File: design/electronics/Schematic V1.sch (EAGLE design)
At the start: 175 parts, among them J1 PJ-202AH, J2 PJ-025, J3 DD50P564GTXLF, J4 DD50P564GTXLF, J5 SAMTEC-TST-105-01-X-DJ, J6 SSW-106-02-TM-S-RA, SW1 TL6330AF200Q, U1 STM32F207VGT6TR, U10 SN65LBC175ADD16-M, U11 MAX7375AXR805+T21-0075D_MXM-M, U12 SN75ALS174ADWRDW20-M, U13 SN75468DRD0016A_M, U14 SN75468DRD0016A_M, U15 ACSL-6400-00TESOIC_6400-00TE-M, U16 ACSL-6400-00TESOIC_6400-00TE-M, U17 SN65LBC175ADD16-M, U18 SN65LBC175ADD16-M, U19 SN65LBC175ADD16-M, U2 LM2678S-5.0/NOPBTS7B-M, U21 RS0104YQTSSOP-14_JRT-M, U22 RS0104YQTSSOP-14_JRT-M, U24 RS0104YQTSSOP-14_JRT-M, U3 CDBC520-GCDBC-G-M, U4 TLV1117LV33DCYR, U5 STM32F207VGT6TR, U6 RS0104YQTSSOP-14_JRT-M, U7 SN75ALS174ADWRDW20-M, U8 OPA4205APWRTSSOP14_PW_R-PDSO-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, U9 TPS63700DRCR

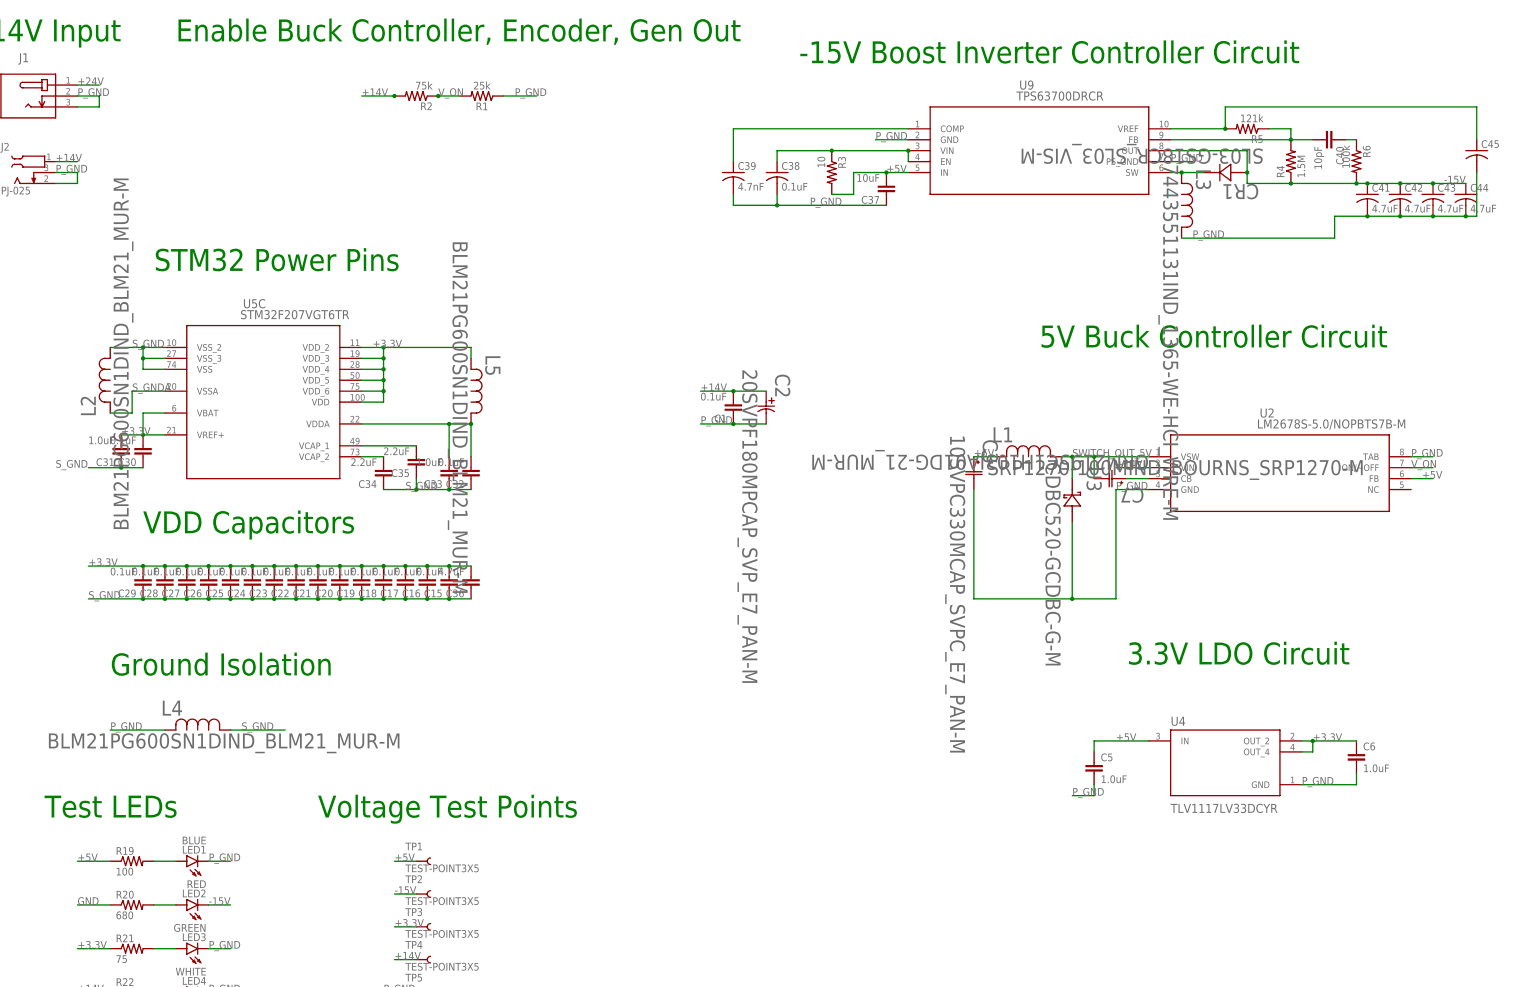
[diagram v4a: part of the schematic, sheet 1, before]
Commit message: Updated Power Circuit Schematic + Layout + Components
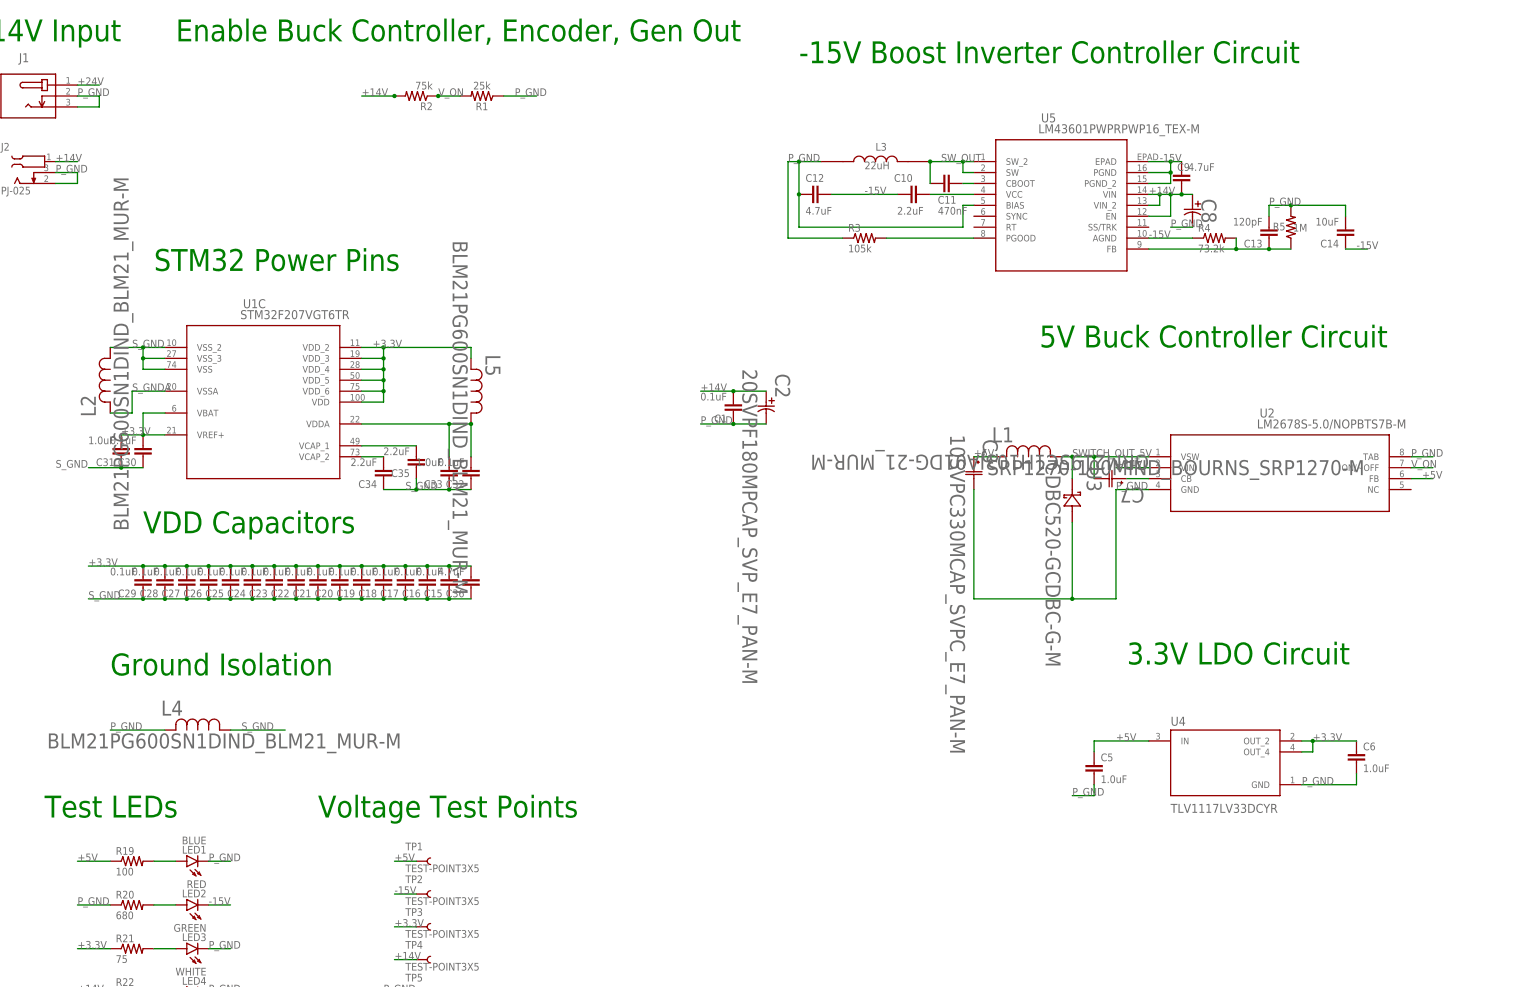
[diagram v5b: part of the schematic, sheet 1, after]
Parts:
- removed C37: 10uF, SparkFun-Capacitors:10UF-0805-10V-10%
- removed C38: 0.1uF, rcl:C-USC0805
- removed C39: 4.7nF, rcl:C-USC0805
- removed C40: 10pF, SparkFun-Capacitors:10UF-0805-10V-10%
- removed C41, C42, C43, C44: 4.7uF, rcl:C-USC0805
- removed C45: (no value), rcl:C-USC0805
- removed CR1: SL03-GS18CR_SL03_VIS-M, SSW-130-01-G-S:SL03-GS18CR_SL03_VIS-M
- removed R6: 100k, rcl:R-US_R0805
- removed U9: TPS63700DRCR, SSW-130-01-G-S:TPS63700DRCR
- added C10: 2.2uF, SparkFun-Capacitors:2.2UF-0805-25V-(+80/-20%)
- added C11: 470nF, SparkFun-Capacitors:470NF-0805-100V-10%-X7S
- added C12, C9: 4.7uF, SparkFun-Capacitors:4.7UF-0805-50V-(10%)
- added C13: 120pF, SparkFun-Capacitors:4.7UF-0805-50V-(10%)
- added C14: 10uF, SparkFun-Capacitors:4.7UF-0805-50V-(10%)
- added C8: 68uF, SSW-130-01-G-S:UWD1V680MCL1GSPCAP_6.3X7.7-ELECT_NCA-M
- L3: value 7443551131IND_1365-WE-HCI_WRE-M -> 22uH; device SSW-130-01-G-S:7443551131IND_1365-WE-HCI_WRE-M -> SSW-130-01-G-S:VLS201610CX-220M-1
- R3: value 10 -> 105k
- R4: value 1.5M -> 73.2k
- R5: value 121k -> 1M
- R69: value (none) -> 10k
- U5: value STM32F207VGT6TR -> LM43601PWPRPWP16_TEX-M; device SSW-130-01-G-S:STM32F207VGT6TR -> SSW-130-01-G-S:LM43601PWPRPWP16_TEX-M
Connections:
- removed net FRWD_EX_TORQUE_LIM_GPIO_1: U1A.PC6
- removed net FRWD_EX_TORQUE_LIM_GPIO_2: U1A.PA11
- removed net GND: R20.1
- removed net N$10: C40.2, R4.2, R5.1, U9.FB
- removed net N$6: C38.1, R3.1, U9.EN, U9.VIN
- removed net N$9: C45.1, R5.2, U9.VREF
- new net SW_OUT: C11.1, L3.2, U5.SW, U5.SW_2
- net +14V: now also C8.1, C9.2, U5.EN, U5.VIN, U5.VIN_2
- net +3.3V: now also U1C.VBAT, U1C.VDD, U1C.VDD_2, U1C.VDD_3, U1C.VDD_4, U1C.VDD_5, U1C.VDD_6, U1C.VREF+; no longer U5C.VBAT, U5C.VDD, U5C.VDD_2, U5C.VDD_3, U5C.VDD_4, U5C.VDD_5, U5C.VDD_6, U5C.VREF+
- net +5V: no longer C37.2, R3.2, U9.IN
- net -15V: now also C10.1, C12.1, C14.1, C9.1, U5.AGND, U5.EPAD, U5.PGND, U5.PGND_2; no longer C41.1, C42.1, C43.1, C44.1, CR1.2, R6.2, U9.OUT
- net EXT_CLK: now also U1B.PH0/OSC_IN
- net FRWD_EX_TORQUE_LIM_EN_GPIO_1: now also U1A.PC6
- net FRWD_EX_TORQUE_LIM_EN_GPIO_2: now also U1A.PA11
- net GEN_PURPOSE_OUT_GPIO_A_2: no longer U19.1Y
- net GEN_PURPOSE_OUT_GPIO_A_2_5V: now also U19.1Y
- net GEN_PURPOSE_OUT_GPIO_B_2: no longer U19.2Y
- net GEN_PURPOSE_OUT_GPIO_B_2_5V: now also U19.2Y
- net GEN_PURPOSE_OUT_GPIO_C_2: no longer U19.3Y
- net GEN_PURPOSE_OUT_GPIO_C_2_5V: now also U19.3Y
- net N$1: now also C10.2, U5.VCC; no longer U1B.PH0/OSC_IN
- net N$11: now also C13.1, R4.2, R5.1, U5.FB; no longer C40.1, R6.1
- net N$14: now also U1C.VDDA; no longer U5C.VDDA
- net N$3: now also C11.2, U5.CBOOT; no longer C39.1, U9.COMP
- net N$4: now also U1C.VCAP_1; no longer U5C.VCAP_1
- net N$5: now also U1C.VCAP_2; no longer U5C.VCAP_2
- net N$7: now also R3.2, U5.PGOOD; no longer CR1.1, L3.2, U9.SW
- net P_GND: now also C12.2, C13.2, C14.2, C8.2, R20.1, R3.1, R5.2, U5.BIAS; no longer C37.1, C38.2, C39.2, C41.2, C42.2, C43.2, C44.2, C45.2, U9.GND, U9.PS_GND
- net SERVO_ALARM_OUT_GPIO_2: no longer U19.4Y
- net SERVO_ALARM_OUT_GPIO_2_5V: now also U19.4Y
- net S_GND: now also U1C.VSS, U1C.VSS_2, U1C.VSS_3; no longer U5C.VSS, U5C.VSS_2, U5C.VSS_3
- net S_GNDA: now also U1C.VSSA; no longer U5C.VSSA
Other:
- moved on the sheet: R3, R4, R5

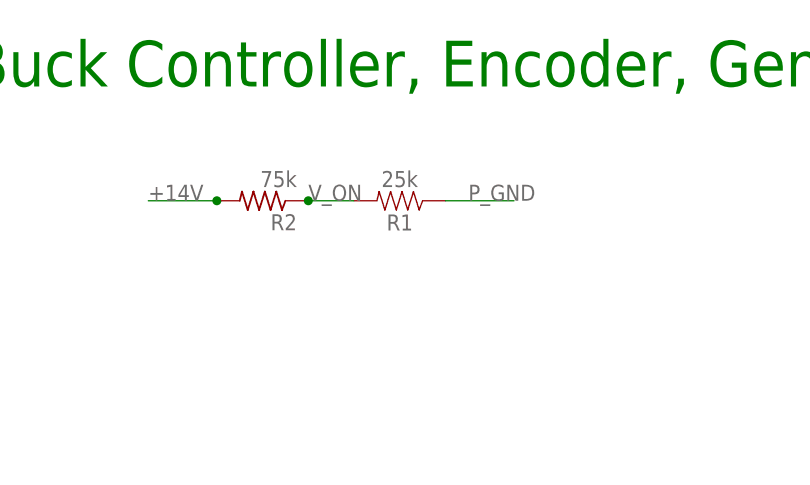
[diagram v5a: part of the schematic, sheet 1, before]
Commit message: Updated Schematic and Board with a few components
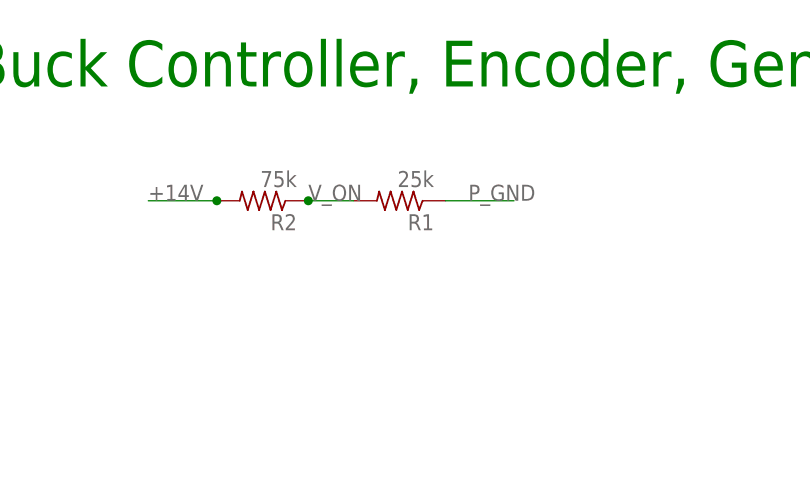
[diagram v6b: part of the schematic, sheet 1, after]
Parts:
- R1: device SparkFun-Resistors:33KOHM-0603-1/10W-1% -> rcl:R-US_R0805
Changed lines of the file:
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@@
 <part name="R15" library="rcl" library_urn="urn:adsk.eagle:library:334" deviceset="R-US_" device="R0805" package3d_urn="urn:adsk.eagle:package:23553/2" value="73k"/>
 <part name="R16" library="rcl" library_urn="urn:adsk.eagle:library:334" deviceset="R-US_" device="R0805" package3d_urn="urn:adsk.eagle:package:23553/2" value="10k"/>
-<part name="R1" library="SparkFun-Resistors" library_urn="urn:adsk.eagle:library:532" deviceset="33KOHM" device="-0603-1/10W-1%" package3d_urn="urn:adsk.eagle:package:39650/1" value="25k"/>
 <part name="R2" library="rcl" library_urn="urn:adsk.eagle:library:334" deviceset="R-US_" device="R0805" package3d_urn="urn:adsk.eagle:package:23553/2" value="75k"/>
 <part name="C46" library="SparkFun-Capacitors" library_urn="urn:adsk.eagle:library:510" deviceset="1.0UF" device="-0805-25V-10%" package3d_urn="urn:adsk.eagle:package:37429/1" value="1.0uF"/>
@@
 <part name="C13" library="SparkFun-Capacitors" deviceset="4.7UF" device="-0805-50V-(10%)" value="120pF"/>
 <part name="C14" library="SparkFun-Capacitors" deviceset="4.7UF" device="-0805-50V-(10%)" value="10uF"/>
+<part name="R1" library="rcl" library_urn="urn:adsk.eagle:library:334" deviceset="R-US_" device="R0805" package3d_urn="urn:adsk.eagle:package:23553/2" value="25k"/>
 </parts>
 <sheets>
@@
 <attribute name="NAME" x="32.1056" y="236.4486" size="2.0828" layer="95" ratio="6" rot="SR0"/>
 </instance>
-<instance part="R1" gate="G$1" x="139.7" y="228.6" smashed="yes" rot="R180">
-<attribute name="NAME" x="139.7" y="227.076" size="1.778" layer="95" font="vector" rot="R180" align="bottom-center"/>
-<attribute name="VALUE" x="139.7" y="230.124" size="1.778" layer="96" font="vector" rot="R180" align="top-center"/>
-</instance>
 <instance part="R2" gate="G$1" x="124.46" y="228.6" smashed="yes" rot="R180">
 <attribute name="NAME" x="128.27" y="227.1014" size="1.778" layer="95" rot="R180"/>
@@
 <attribute name="NAME" x="338.836" y="195.199" size="1.778" layer="95" font="vector" rot="R180"/>
 <attribute name="VALUE" x="338.836" y="200.279" size="1.778" layer="96" font="vector" rot="R180"/>
+</instance>
+<instance part="R1" gate="G$1" x="139.7" y="228.6" smashed="yes" rot="R180">
+<attribute name="NAME" x="143.51" y="227.1014" size="1.778" layer="95" rot="R180"/>
+<attribute name="VALUE" x="143.51" y="231.902" size="1.778" layer="96" rot="R180"/>
 </instance>
 </instances>
@@
 </segment>
 <segment>
-<pinref part="R1" gate="G$1" pin="1"/>
 <wire x1="144.78" y1="228.6" x2="152.4" y2="228.6" width="0.1524" layer="91"/>
 <label x="147.32" y="228.6" size="1.778" layer="95"/>
+<pinref part="R1" gate="G$1" pin="1"/>
 </segment>
 <segment>
@@
 </segment>
 <segment>
-<pinref part="R1" gate="G$1" pin="2"/>
 <wire x1="129.54" y1="228.6" x2="134.62" y2="228.6" width="0.1524" layer="91"/>
 <label x="129.54" y="228.6" size="1.778" layer="95"/>
 <pinref part="R2" gate="G$1" pin="1"/>
 <junction x="129.54" y="228.6"/>
+<pinref part="R1" gate="G$1" pin="2"/>
 </segment>
 </net>

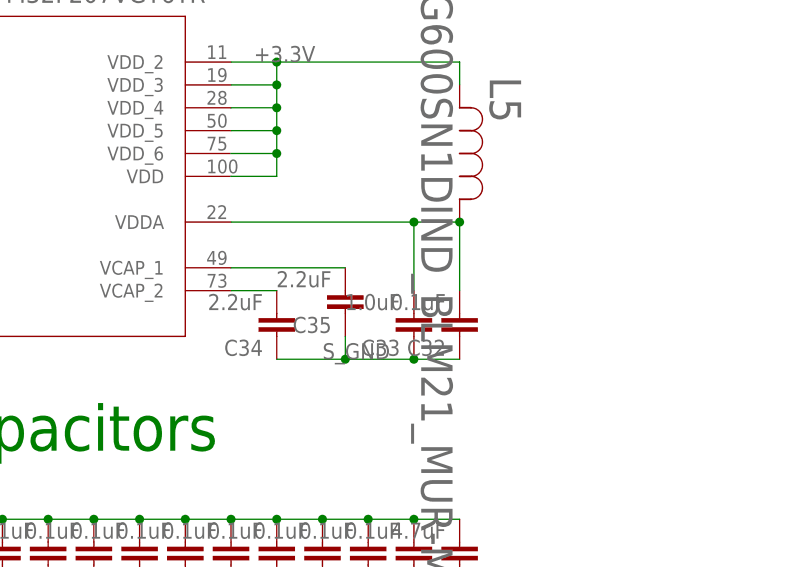
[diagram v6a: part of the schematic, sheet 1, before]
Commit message: Updated Power Scheme of STM32
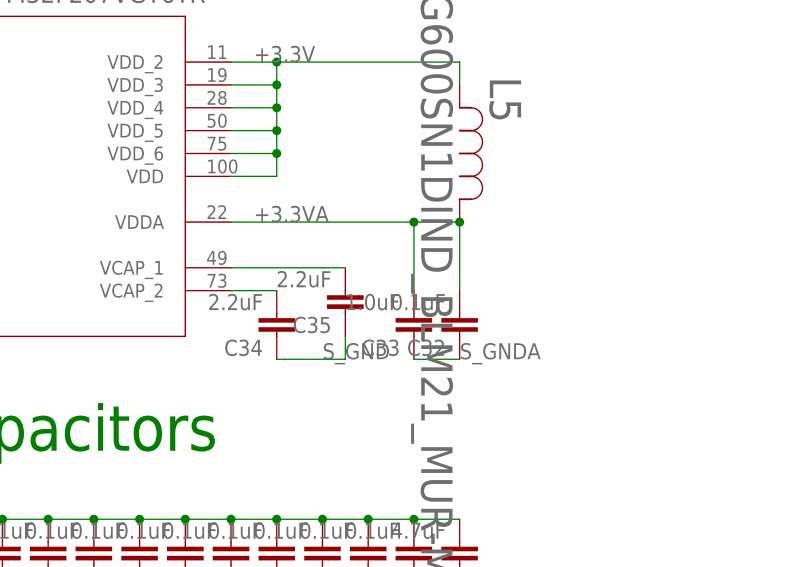
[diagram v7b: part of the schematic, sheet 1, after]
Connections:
- net N$14 renamed +3.3VA
- net S_GND: no longer C32.1, C33.1
- net S_GNDA: now also C32.1, C33.1
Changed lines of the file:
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@@
 <wire x1="124.46" y1="137.16" x2="116.84" y2="137.16" width="0.1524" layer="91"/>
 <label x="121.92" y="137.16" size="1.778" layer="95"/>
-<pinref part="C32" gate="G$1" pin="1"/>
-<wire x1="132.08" y1="137.16" x2="124.46" y2="137.16" width="0.1524" layer="91"/>
-<wire x1="132.08" y1="137.16" x2="137.16" y2="137.16" width="0.1524" layer="91"/>
-<pinref part="C33" gate="G$1" pin="1"/>
-<junction x="132.08" y="137.16"/>
-<junction x="124.46" y="137.16"/>
 </segment>
 <segment>
@@
 <pinref part="U1" gate="C" pin="VSSA"/>
 </segment>
+<segment>
+<pinref part="C32" gate="G$1" pin="1"/>
+<wire x1="132.08" y1="137.16" x2="137.16" y2="137.16" width="0.1524" layer="91"/>
+<pinref part="C33" gate="G$1" pin="1"/>
+<label x="137.16" y="137.16" size="1.778" layer="95"/>
+</segment>
 </net>
-<net name="N$14" class="0">
+<net name="+3.3VA" class="0">
 <segment>
 <pinref part="C32" gate="G$1" pin="2"/>
@@
 <junction x="137.16" y="152.4"/>
 <pinref part="U1" gate="C" pin="VDDA"/>
+<label x="114.3" y="152.4" size="1.778" layer="95"/>
 </segment>
 </net>
